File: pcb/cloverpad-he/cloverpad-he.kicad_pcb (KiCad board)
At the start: 2 copper layers, 70 x 70 mm, 65 parts, among them J1 USB_C_Receptacle_USB2.0, SW1 SW_Push, SW2 SW_Push, U1 SRV05-4, U2 XC6206P332MR, U3 DRV5056A4xDBZxQ1, U4 DRV5056A4xDBZxQ1, U5 DRV5056A4xDBZxQ1, U6 74AHCT1G125, U7 74AHCT1G125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

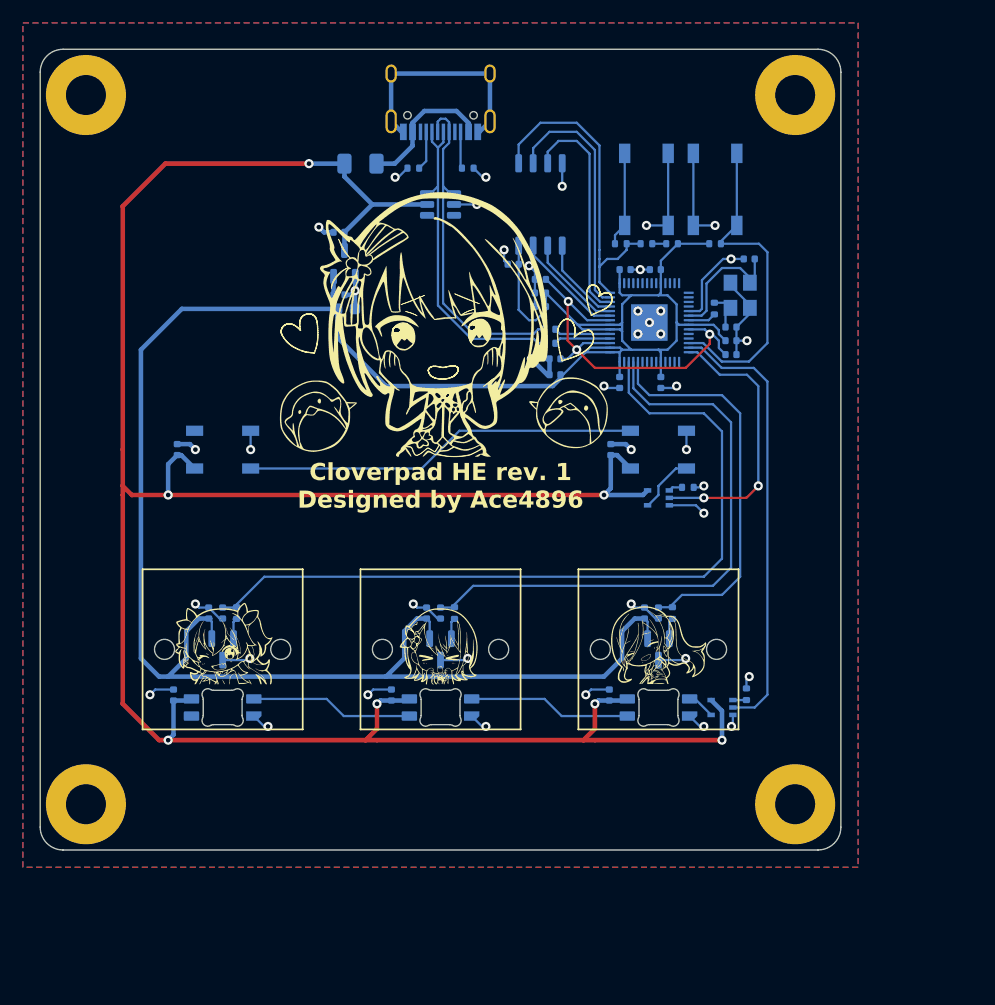
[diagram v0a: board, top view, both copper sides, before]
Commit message: chore: remove rgb from Cloverpad HE pcb
I want to keep the cost down; including RGB means that standard PCB assembly is needed, which causes the price to spike...
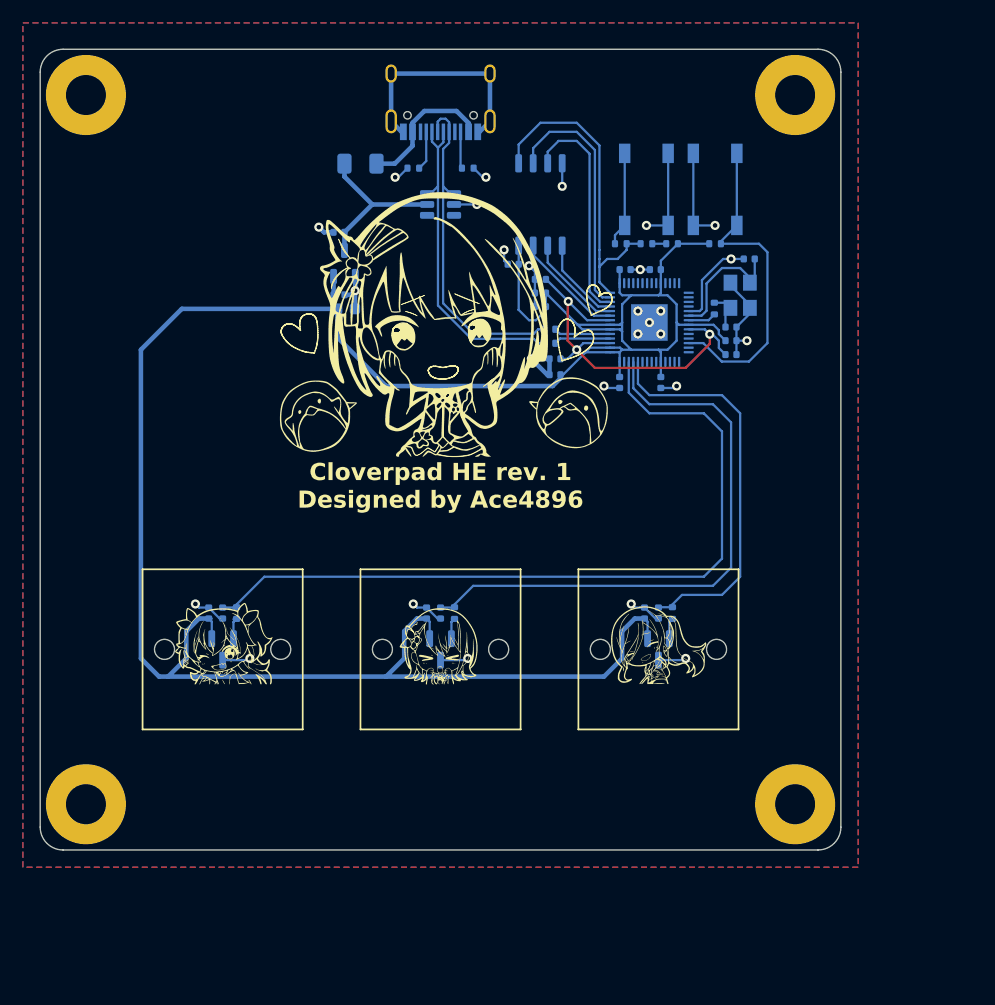
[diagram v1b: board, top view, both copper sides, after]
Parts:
- removed C10, C11, C26, C27, C9: 100nF, Capacitor_SMD:C_0402_1005Metric
- removed D1, D2: WS2812B, LED_SMD:LED_WS2812B_PLCC4_5.0x5.0mm_P3.2mm
- removed LED1, LED2, LED3: SK6812MINI-E, PCM_marbastlib-mx:LED_MX_6028R
- removed R6, R8: 1k, Resistor_SMD:R_0402_1005Metric
- removed U6, U7: 74AHCT1G125, Package_TO_SOT_SMD:SOT-353_SC-70-5
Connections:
- U8 pad 27: RGB_HS -> unconnected-(U8-GPIO16-Pad27)
- U8 pad 28: RGB_GLOW -> unconnected-(U8-GPIO17-Pad28)
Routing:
- net +5V: track 213.0 -> 14.4 mm, vias 7 -> 0
- net RGB_HS: track 39.0 -> 0.00 mm
- net Net-(D1-DOUT): track 34.6 -> 0.00 mm
- net GND: track 121.3 -> 96.2 mm, vias 41 -> 27
- net RGB_GLOW: track 24.3 -> 0.00 mm, vias 2 -> 0
- net Net-(LED2-DOUT): track 14.2 -> 0.00 mm
- net Net-(LED1-DOUT): track 14.2 -> 0.00 mm
- net Net-(D1-DIN): track 5.20 -> 0.00 mm
- net Net-(LED1-DIN): track 2.46 -> 0.00 mm
- net Net-(R8-Pad1): track 1.22 -> 0.00 mm
- net Net-(R6-Pad1): track 1.18 -> 0.00 mm

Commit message: fix: swap positions of HS0 and HS2 on cloverpad he
same as on cloverpad mx - this puts HS0 on the leftmost side.
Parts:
- moved C3 38.1 mm to (68.6, 65.1)
- moved C8 38.1 mm to (69.9, 65.1)
- moved U3 38.1 mm to (31.7, 68.3)
- moved U5 38.1 mm to (69.9, 68.3)
- moved C1 38.1 mm to (30.5, 65.1)
- moved C6 38.1 mm to (31.8, 65.1)
- moved R3 38.1 mm to (33.0, 65.1)
- moved R5 38.1 mm to (71.0, 65.1)
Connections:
- U8 pad 38: HS0 -> HS2
- U8 pad 40: HS2 -> HS0
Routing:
- net HS2: track 69.0 -> 34.6 mm
- net HS0: track 34.6 -> 69.0 mm

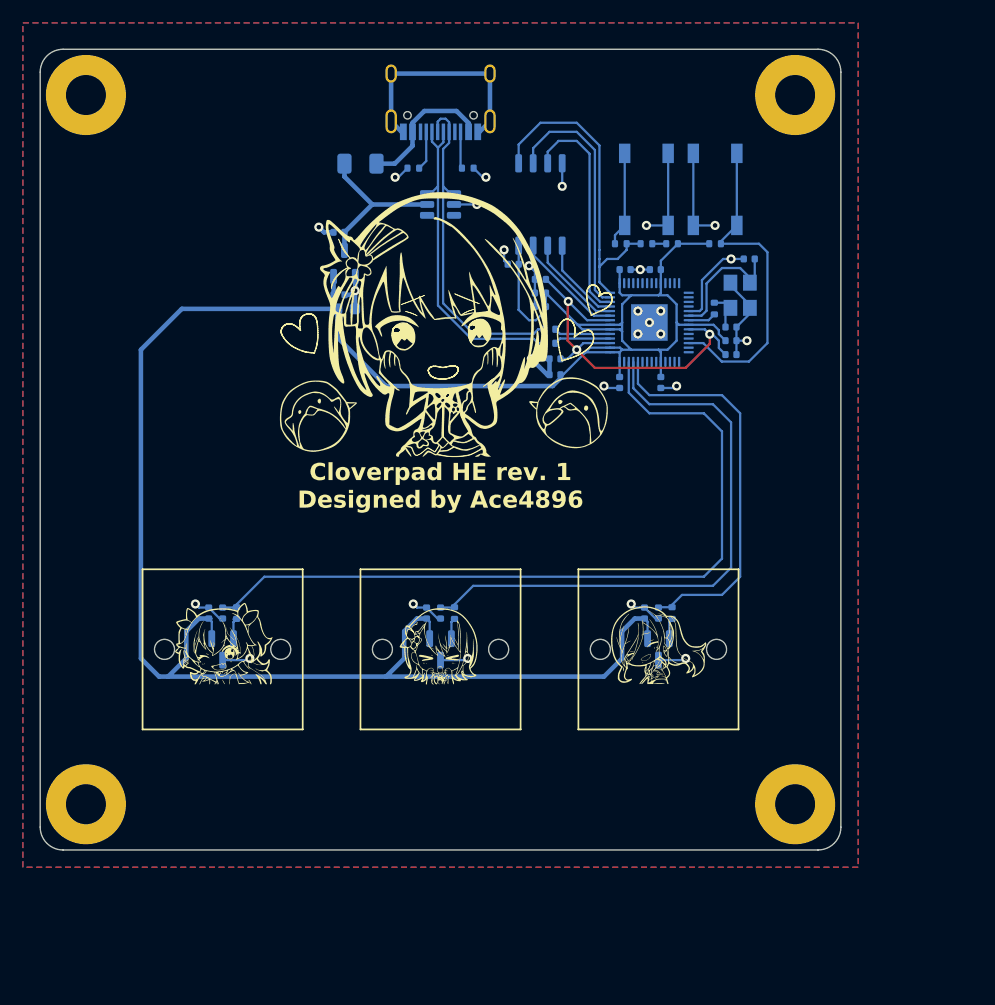
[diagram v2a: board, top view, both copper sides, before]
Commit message: fix: port pcb size changes to cloverpad he
since there's no RGB now, it's possible to route the analog signals more directly.
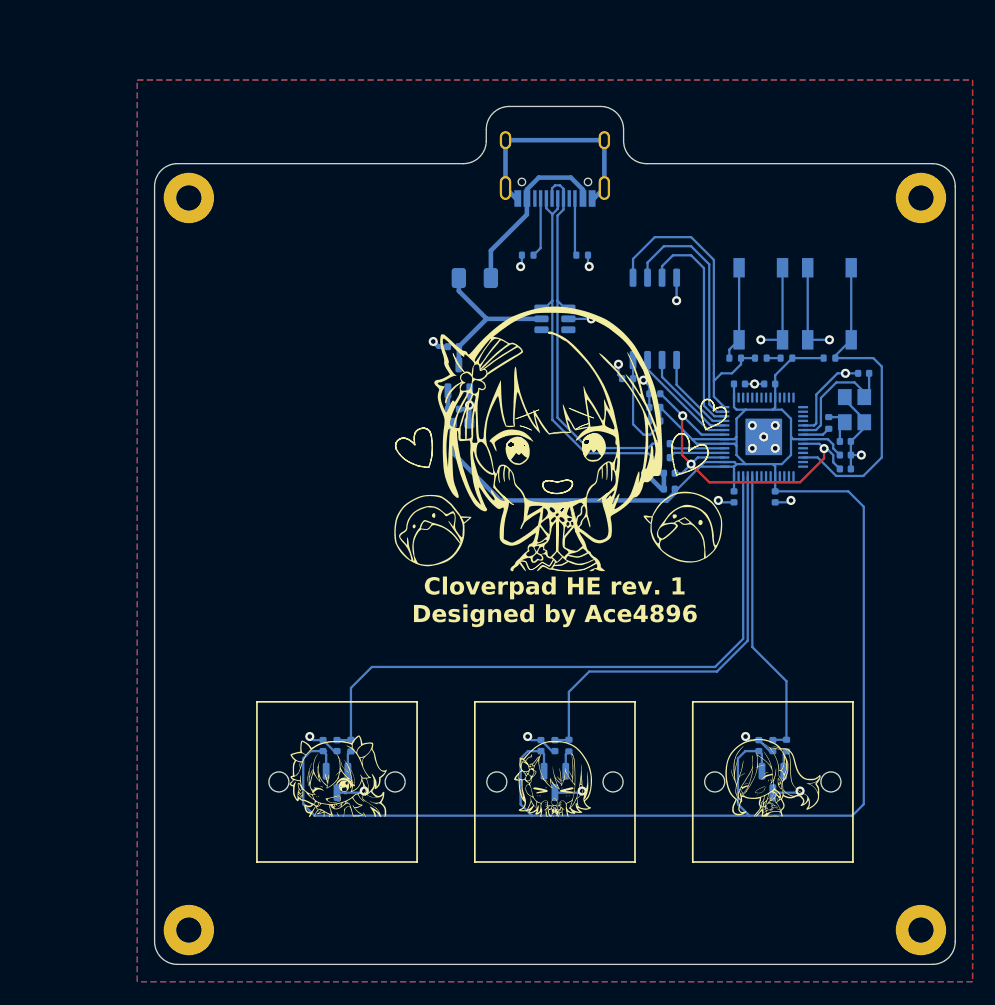
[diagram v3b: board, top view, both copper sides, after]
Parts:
- H1, H2, H3, H4: footprint MountingHole:MountingHole_3.5mm_Pad -> MountingHole:MountingHole_2.2mm_M2_Pad
- moved H4 15.6 mm to (92.8, 92.8)
- moved C1 15.3 mm to (40.5, 76.7)
- moved C2 15.3 mm to (59.6, 76.7)
- moved C3 15.3 mm to (78.6, 76.7)
- moved C6 15.3 mm to (41.8, 76.7)
- moved C7 15.3 mm to (60.8, 76.7)
- moved C8 15.3 mm to (79.9, 76.7)
- moved R3 15.3 mm to (43.0, 76.7)
- moved R4 15.3 mm to (62.0, 76.7)
- moved R5 15.3 mm to (81.0, 76.7)
- moved U4 15.3 mm to (60.8, 79.8)
- moved U5 15.3 mm to (79.9, 79.8)
- moved U3 15.3 mm to (41.7, 79.8)
- moved H2 14.2 mm to (92.8, 28.8)
- moved H3 14.2 mm to (28.8, 92.8)
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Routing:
- net HS1: track 51.8 -> 37.3 mm
- net HS0: track 69.0 -> 56.0 mm
- net HS2: track 34.6 -> 25.5 mm
- net D+: track 29.4 -> 33.6 mm
- net D-: track 28.8 -> 33.0 mm
- net VBUS: track 12.3 -> 15.6 mm
- net +3V3: track 211.7 -> 208.9 mm
- net Net-(J1-CC2): track 3.22 -> 5.01 mm
- net Net-(J1-CC1): track 3.43 -> 5.21 mm
- net GND: track 96.2 -> 95.4 mm
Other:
- board size 70 x 70 mm -> 70 x 75 mm
